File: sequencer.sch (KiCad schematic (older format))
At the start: 159 parts

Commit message: adding extra LEDs for instrument selector
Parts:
- added C?: 0.1µ, ~, symbol C_US
- added D?: LC, symbol LED
- added D?: HC, symbol LED
- added D?: MC, symbol LED
- added D?: CL, symbol LED
- added D?: MA, symbol LED
- added R? (x8): 470, ~, symbol R_US
- added U?: 74AC595, symbol 74AC595
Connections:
- wire segments 481 -> 652
- no-connect marks 12 -> 14
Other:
- moved on the sheet: D?

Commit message: finished adding new LEDs. Could compress all SPI triggers and LEDs into 6 74HC595s instead of 7. Need to think more about layout to decide if this is worthwhile
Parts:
- removed R? (x3): 470, ~, symbol R_US
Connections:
- wire segments 652 -> 636
- no-connect marks 14 -> 16
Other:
- note added: "SPI LED LATCH 5"
- moved on the sheet: C?, D?, R?, U?

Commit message: adjustments to interface changes number of switches and LEDs in SPI network
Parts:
- removed R? (x3): 10K, ~, symbol R_US
- removed SW?: ALT_KEY, symbol TACT_SWITCH
- removed SW?: PRE_SCALE, symbol TACT_SWITCH
- removed SW?: BASIC_VAR, symbol SP3T
- removed SW?: IF_VAR, symbol SPST
- added D?: IF_VAR_A, symbol LED
- added D?: IF_VAR_B, symbol LED
- added R? (x2): 470, ~, symbol R_US
- added SW?: IF_VAR, symbol TACT_SWITCH
- added SW?: BASIC_VAR_A, symbol TACT_SWITCH
- added SW?: BASIC_VAR_B, symbol TACT_SWITCH
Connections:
- wire segments 636 -> 509
- no-connect marks 16 -> 18
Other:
- note added: "1. DIN SYNC IN/OUT\n2. MIDI IN\n3. MIDI OUT"
- moved on the sheet: SW?

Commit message: entire project annotaed, duplicate references fixed with '-1' suffix
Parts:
- gave numbers to parts that had none: 171

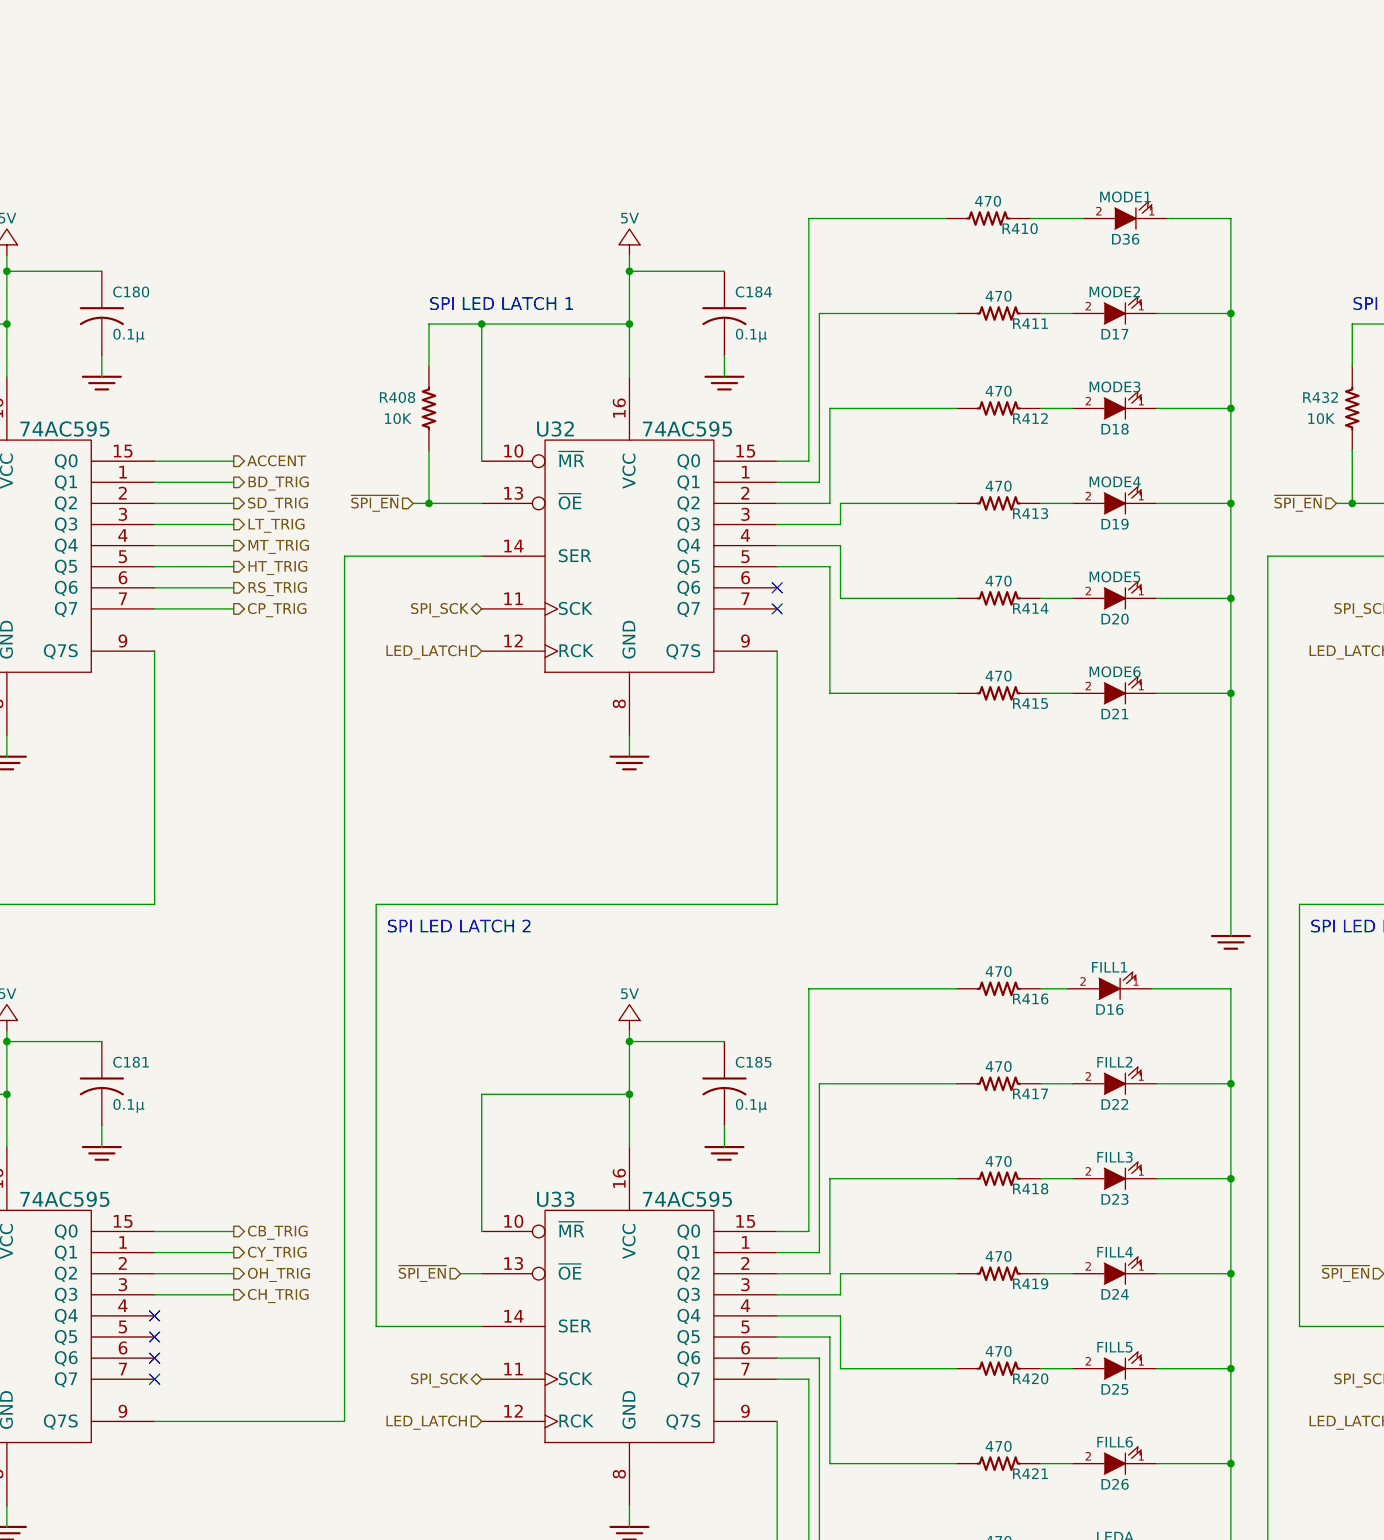
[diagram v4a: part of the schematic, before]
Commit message: adding CD4053 switch lines to SPI outputs
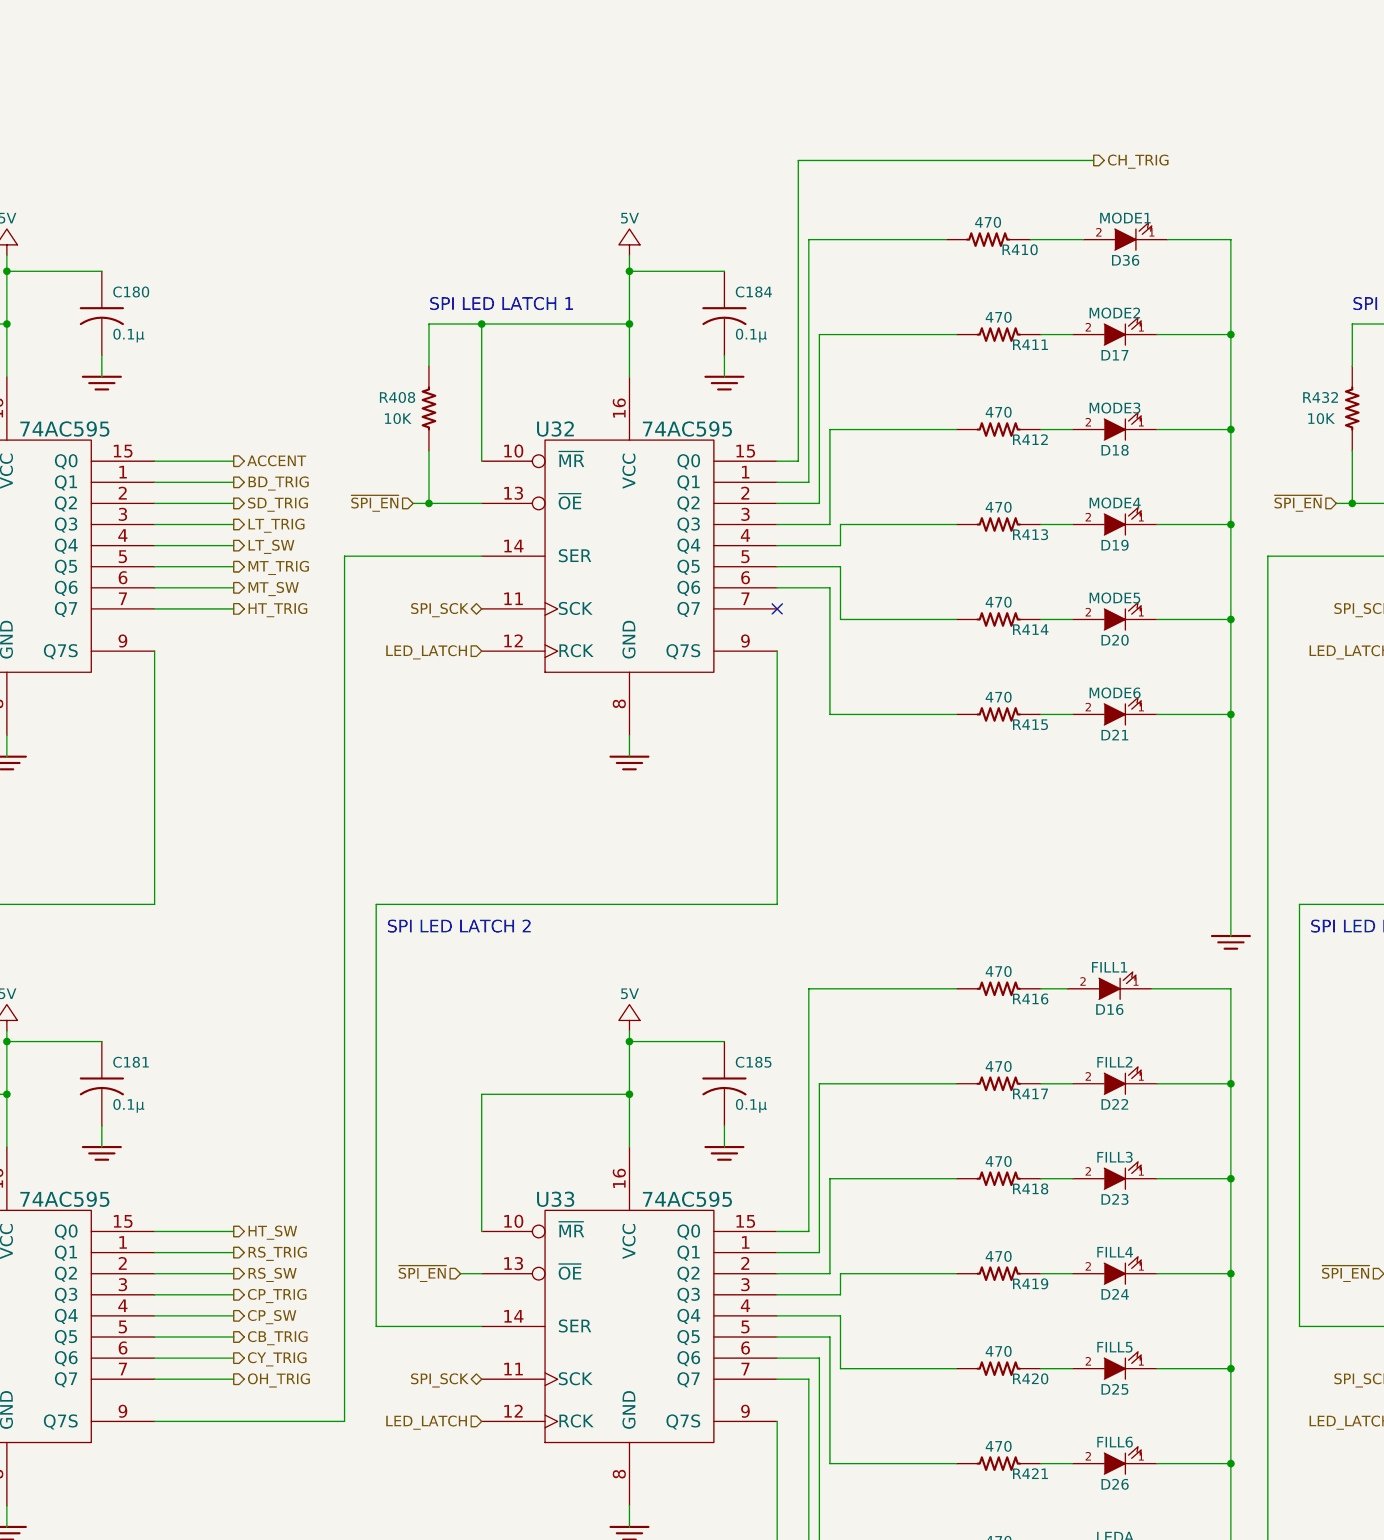
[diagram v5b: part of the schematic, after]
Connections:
- net CB_TRIG: now also U31.5 (Q5); no longer U31.15 (Q0)
- net CH_TRIG: now also U32.15 (Q0); no longer U31.3 (Q3)
- net CP_TRIG: now also U31.3 (Q3); no longer U30.7 (Q7)
- net CY_TRIG: now also U31.6 (Q6); no longer U31.1 (Q1)
- net HT_TRIG: now also U30.7 (Q7); no longer U30.5 (Q5)
- net MT_TRIG: now also U30.5 (Q5); no longer U30.4 (Q4)
- net OH_TRIG: now also U31.7 (Q7); no longer U31.2 (Q2)
- net RS_TRIG: now also U31.1 (Q1); no longer U30.6 (Q6)
- net CP_SW: now reaches U31.4 (Q4)
- net at R412.2: now also U32.3 (Q3); no longer U32.2 (Q2)
- net at R411.2: now also U32.2 (Q2); no longer U32.1 (Q1)
- net at R415.2: now also U32.6 (Q6); no longer U32.5 (Q5)
- net at R414.2: now also U32.5 (Q5); no longer U32.4 (Q4)
- net at R413.2: now also U32.4 (Q4); no longer U32.3 (Q3)
- net at R410.2: now also U32.1 (Q1); no longer U32.15 (Q0)
- new net HT_SW: U31.15 (Q0)
- new net LT_SW: U30.4 (Q4)
- new net MT_SW: U30.6 (Q6)
- new net RS_SW: U31.2 (Q2)
- no-connect marks 18 -> 13
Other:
- moved on the sheet: D17, D18, D19, D20, D21, D36, R410, R411, R412, R413, R414, R415

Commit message: ERC done, 7 warnings that check out
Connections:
- net UART TX is gone; now on net UART_TX: SW1.7
- net GND: now also D50.1 (K), D51.1 (K)
- net UART RX renamed UART_RX
- no-connect marks 13 -> 14
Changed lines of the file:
@@
 $EndComp
 Text GLabel 6325 2425 2    60   Output ~ 0
-UART RX
+UART_RX
 $Comp
 L R_US R398
@@
 ~RESET
 Text GLabel 12700 3175 2    50   Input ~ 0
-UART RX
+UART_RX
 $Comp
 L 5V #PWR0419
@@
 Connection ~ 8250 7875
 Connection ~ 8250 8675
-Text GLabel 9825 7700 0    50   Input ~ 0
-SPI_MOSI
 $Comp
 L R_US R407
@@
 Connection ~ 10525 10000
 Text GLabel 3200 1350 0    60   Input ~ 0
-UART TX
+UART_TX
 $Comp
 L MIDI_DIN X1
@@
 Wire Wire Line
 	14275 7250 14175 7250
+NoConn ~ 2000 1550
+Text GLabel 9825 7700 0    50   Input ~ 0
+SPI_MOSI
+Connection ~ 20700 12400
+Connection ~ 20700 12850
 $EndSCHEMATC

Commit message: netlist exported, starting footprint assignment
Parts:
- C172, C173, C174, C175, C176, C177, C178, C179, C180, C181, C184, C185, C186, C187, C190, C191: footprint ~ -> MyModules:SM0603-C-JRL
- C182, C183: footprint (none) -> MyModules:SM0603-C-JRL
- C188, C189: footprint ~ -> MyModules:2MM-POL-CAP
- D15: footprint (none) -> MyModules:SOD323-C1A2
- D16, D17, D18, D19, D20, D21, D22, D23, D24, D25, D26, D27, D28, D29, D30, D31, D32, D33, D34, D35, D36, D37, D38, D39, D40, D41, D42, D43, D44, D45, D46, D47, D48, D49, D50, D51, D72: footprint (none) -> MyModules:3MM-LED-C1A2
- IC1: footprint TQFP32 -> Housings_QFP:TQFP-32_7x7mm_Pitch0.8mm
- IC2: footprint TSSOP8 -> MyModules:TSSOP8-JRL
- ISP1: footprint (none) -> synth:CONN-2X3-0100R
- L1: footprint (none) -> MyModules:SM0805-HAND
- OC1: footprint optocoupler-DIL08 -> MyModules:6-SMD
- R384, R385, R386, R387, R388, R389, R390, R391, R392, R393, R394, R395, R396, R397, R398, R399, R400, R401, R402, R403, R404, R405, R406, R407, R408, R409, R410, R411, R412, R413, R414, R415, R416, R417, R418, R419, R420, R421, R422, R423, R424, R425, R426, R427, R428, R429, R430, R431, R432, R433, R434, R435, R436, R437, R438, R439, R440, R441, R442, R443, R444, R445, R446, R447, R448, R449, R450, TP16, TP17, X1: footprint ~ -> (none)

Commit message: all parts assinged except MIDI jack
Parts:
- R384, R385, R386, R387, R388, R389, R390, R391, R392, R393, R394, R395, R396, R397, R398, R399, R400, R401, R402, R403, R404, R405, R406, R407, R408, R409, R410, R411, R412, R413, R414, R415, R416, R417, R418, R419, R420, R421, R422, R423, R424, R425, R426, R427, R428, R429, R430, R431, R432, R433, R434, R435, R436, R437, R438, R439, R440, R441, R442, R443, R444, R445, R446, R447, R448, R449, R450: footprint (none) -> MyModules:SM0603-R-JRL
- SW1: footprint (none) -> MyModules:SS-23E02-2P3T-SLIDE
- SW10, SW11, SW13, SW14, SW15, SW16, SW17, SW18, SW19, SW20, SW4, SW5, SW7, SW8, SW9: footprint (none) -> MyModules:KS-01Q-02-SPST
- SW12, SW2, SW3, SW6: footprint (none) -> MyModules:B3F-1050-OMRON
- SW21, SW22: footprint (none) -> MyModules:CHERRY-MX
- TP15, TP16, TP17, TP18, TP19: footprint (none) -> MyModules:TEST_POINT_LOOP_4592
- U27, U28, U29, U30, U31, U32, U33, U34, U36, U37: footprint (none) -> Housings_SSOP:TSSOP-16_4.4x5mm_Pitch0.65mm
- U35: footprint (none) -> MyModules:R-78E-0.5
- VR18: value TEMPO -> 10K; footprint (none) -> MyModules:RD901F-ALPHA-POT
- Y1: footprint (none) -> synth:403-XTAL-4-SMD
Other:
- note added: "TEMPO"
